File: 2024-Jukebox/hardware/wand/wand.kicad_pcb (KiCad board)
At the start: 2 copper layers, 40.7 x 32 mm, 48 parts, among them J1 USB_C_Receptacle_USB2.0, J2 Conn_01x05, J3 Conn_01x04, J4 Conn_01x04, J5 Conn_01x04, J6 Conn_01x01, J7 Conn_01x04, Q1 MUN5214DW1T1G, Q2 BSS138, Q3 CJ3139K, Q5 BSS138, SW1 SW_SPDT, U1 CP2104, U2 ESP32-PICO-D4, U3 ICM-20948, U4 TP4065-4.2V, U5 MIC5225-3.3, U6 LY68L6400SLIT, U7 MIC5225-1.8

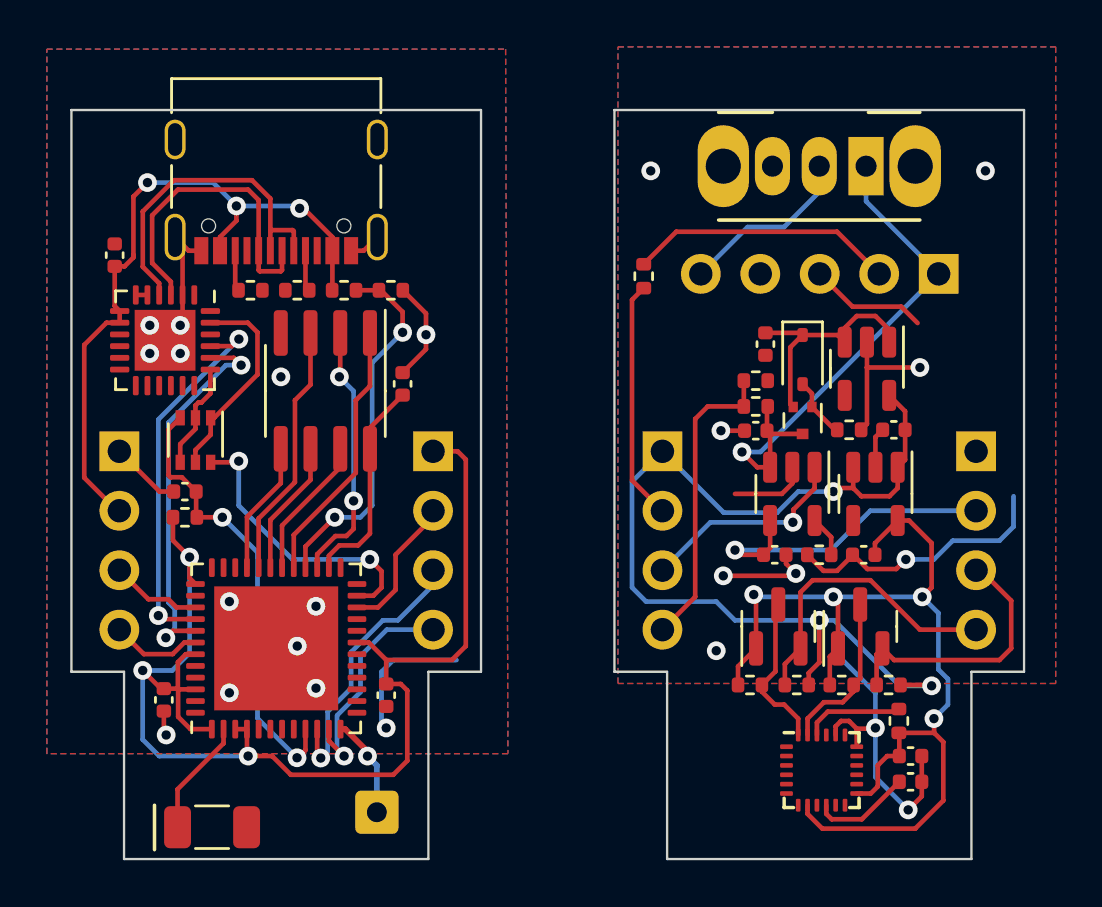
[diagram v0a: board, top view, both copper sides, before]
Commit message: Added wand production files
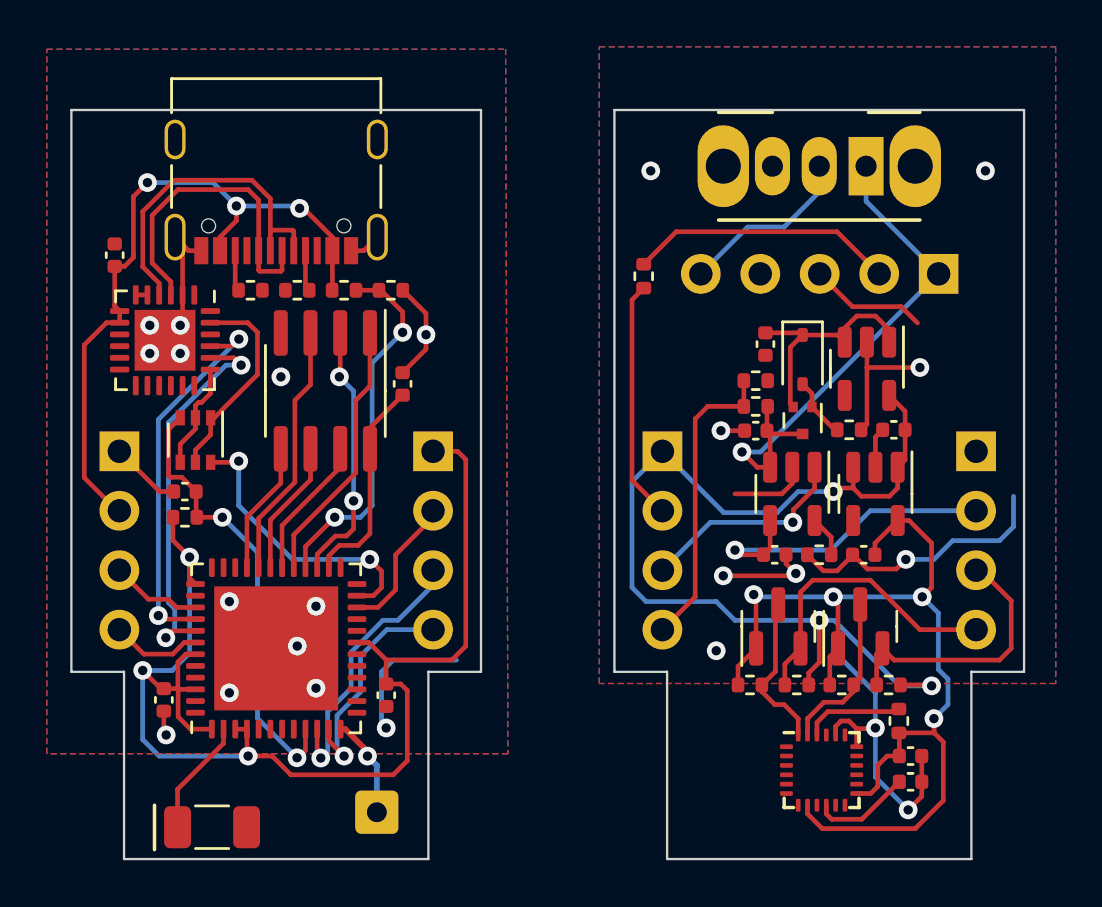
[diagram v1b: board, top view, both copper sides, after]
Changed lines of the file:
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@@
         (xy 41.299266 -2.7)
         (xy 41.3 24.5)
-        (xy 22.6 24.5)
-        (xy 22.6 -2.7)
+        (xy 21.8 24.5)
+        (xy 21.8 -2.7)
       )
     )

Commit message: Changed 3.3v regulator
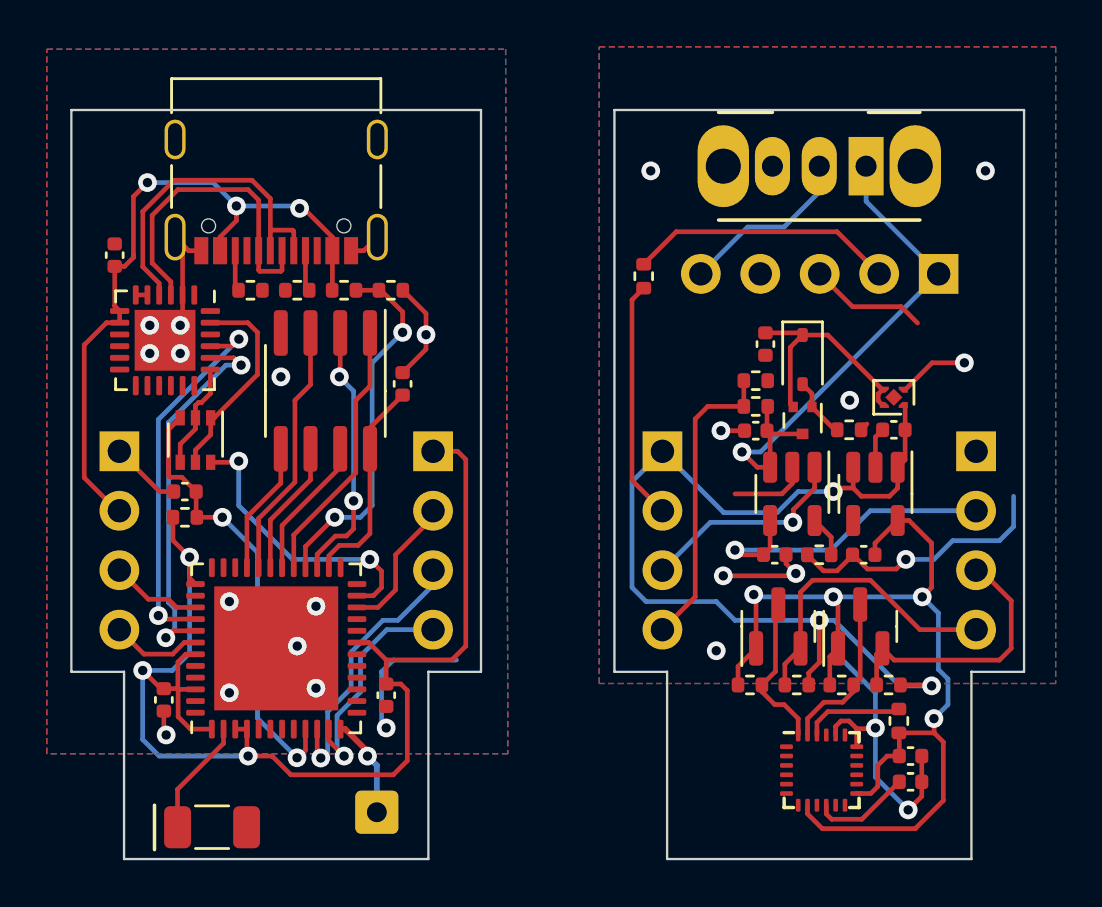
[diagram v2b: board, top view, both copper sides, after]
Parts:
- R4: value 442k -> 100k
- R5: value 160k -> 33k
- U5: value MIC5225-3.3 -> NCP167BMX330TBG; footprint Package_TO_SOT_SMD:SOT-23-5 -> Package_DFN_QFN:OnSemi_XDFN4-1EP_1.0x1.0mm_EP0.52x0.52mm
- moved U5 1.67 mm to (34.4, 12.3), turned to 180 degrees
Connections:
- U5 pad 1: Net-(D1-K) -> +3V3
- U5 pad 4: unconnected-(U5-BP-Pad4) -> Net-(D1-K)
- U5 pad 5: +3V3 -> (no net)
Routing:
- net GND: track 67.3 -> 64.5 mm, vias 23 -> 24
- net +3V3: track 96.2 -> 95.4 mm
